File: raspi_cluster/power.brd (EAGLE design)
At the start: 28.9 x 34.3 mm, 5 parts

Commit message: made the printable pcb design
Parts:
- added 5V1, 5V2, 5V3, 5V4, 5V5: 22-23-2051, con-molex:22-23-2051
- added LED1, LED2, LED3, LED4, LED5: (no value), eagle-ltspice:LED_LD260
- added R1, R2, R3, R4, R5: (no value), resistor:0204/7
- added RASPI1, RASPI2, RASPI3, RASPI4, RASPI5: (no value), jumper:JP6Q
- added TYBG1, TYBG2, TYBG3, TYBG4, TYBG5: FUSEPICOFUSE, fuse:PICOFUSE
- moved TYBG 55.1 mm to (18.4, 11.1)
- moved 5V 55.1 mm to (8.26, 7.30)
- moved LED 55.1 mm to (4.45, 23.8)
- moved R 55.1 mm to (13.3, 23.8)
- moved RASPI 55.1 mm to (6.99, 14.9)
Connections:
- new net N$10: RASPI1.11, TYBG1.1
- new net N$11: 5V1.4, 5V1.5, RASPI1.7
- new net N$12: R1.2, RASPI1.12
- new net N$13: 5V2.1, 5V2.2, TYBG2.2
- new net N$14: LED2.A, R2.1
- new net N$15: LED2.K, RASPI2.8
- new net N$16: RASPI2.11, TYBG2.1
- new net N$17: 5V2.4, 5V2.5, RASPI2.7
- new net N$18: R2.2, RASPI2.12
- new net N$19: 5V3.1, 5V3.2, TYBG3.2
- new net N$20: LED3.A, R3.1
- new net N$21: LED3.K, RASPI3.8
- new net N$22: RASPI3.11, TYBG3.1
- new net N$23: 5V3.4, 5V3.5, RASPI3.7
- new net N$24: R3.2, RASPI3.12
- new net N$25: 5V4.1, 5V4.2, TYBG4.2
- new net N$26: LED4.A, R4.1
- new net N$27: LED4.K, RASPI4.8
- new net N$28: RASPI4.11, TYBG4.1
- new net N$29: 5V4.4, 5V4.5, RASPI4.7
- new net N$30: R4.2, RASPI4.12
- new net N$31: 5V5.1, 5V5.2, TYBG5.2
- new net N$32: LED5.A, R5.1
- new net N$33: LED5.K, RASPI5.8
- new net N$34: RASPI5.11, TYBG5.1
- new net N$35: 5V5.4, 5V5.5, RASPI5.7
- new net N$36: R5.2, RASPI5.12
- new net N$7: 5V1.1, 5V1.2, TYBG1.2
- new net N$8: LED1.A, R1.1
- new net N$9: LED1.K, RASPI1.8
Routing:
- net N$33: track 0.00 -> 11.7 mm, vias 0 -> 1
- net N$15: track 0.00 -> 11.7 mm, vias 0 -> 1
- net N$9: track 0.00 -> 11.7 mm, vias 0 -> 1
- net N$27: track 0.00 -> 11.7 mm, vias 0 -> 1
- net N$21: track 0.00 -> 11.7 mm, vias 0 -> 1
- net N$36: track 0.00 -> 9.94 mm
- net N$24: track 0.00 -> 9.94 mm
- net N$18: track 0.00 -> 9.94 mm
- net N$30: track 0.00 -> 9.94 mm
- net N$12: track 0.00 -> 9.94 mm
- net N$17: track 0.00 -> 9.36 mm
- net N$35: track 0.00 -> 9.36 mm
- net N$11: track 0.00 -> 9.36 mm
- net N$29: track 0.00 -> 9.36 mm
- net N$23: track 0.00 -> 9.36 mm
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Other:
- board size 28.9 x 34.3 mm -> 87.3 x 68.9 mm
- board text removed: "db tech"
- board text removed: "printed with love"

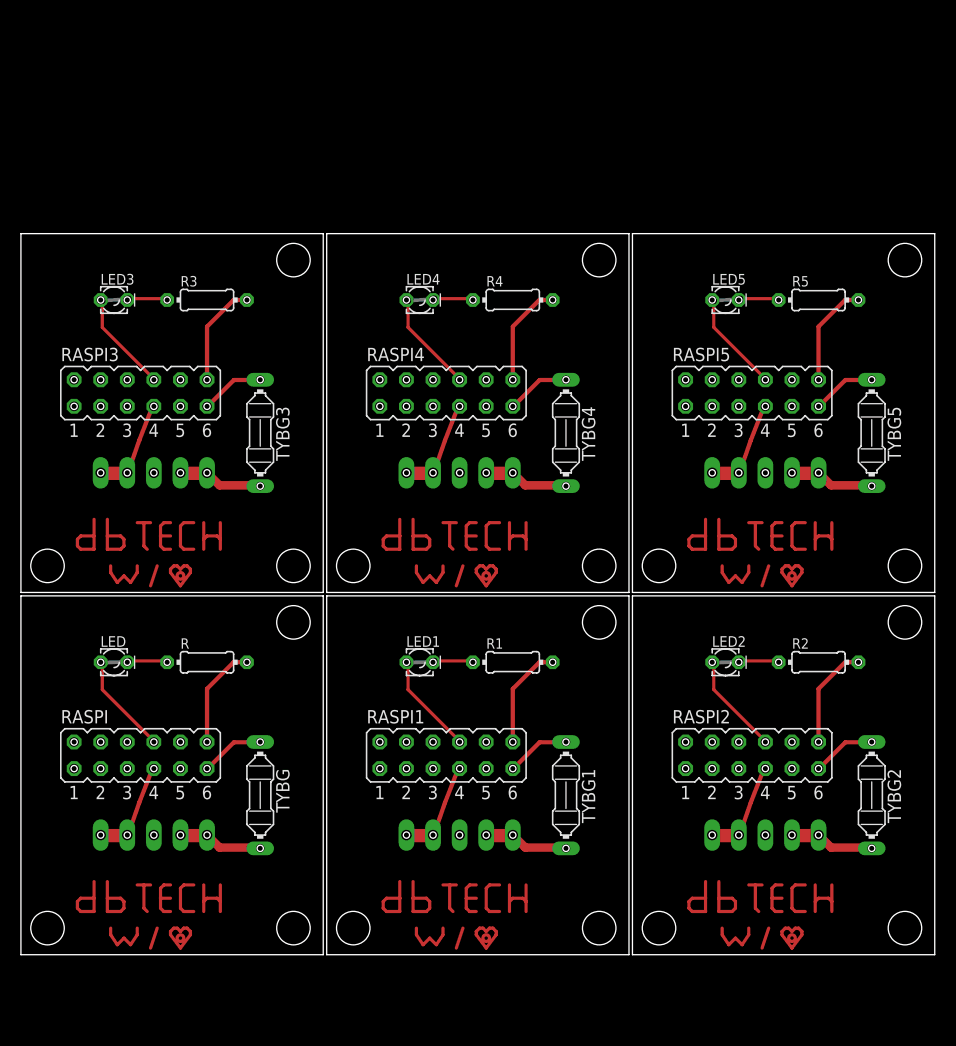
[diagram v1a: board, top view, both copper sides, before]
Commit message: updated power schematic for breakout board
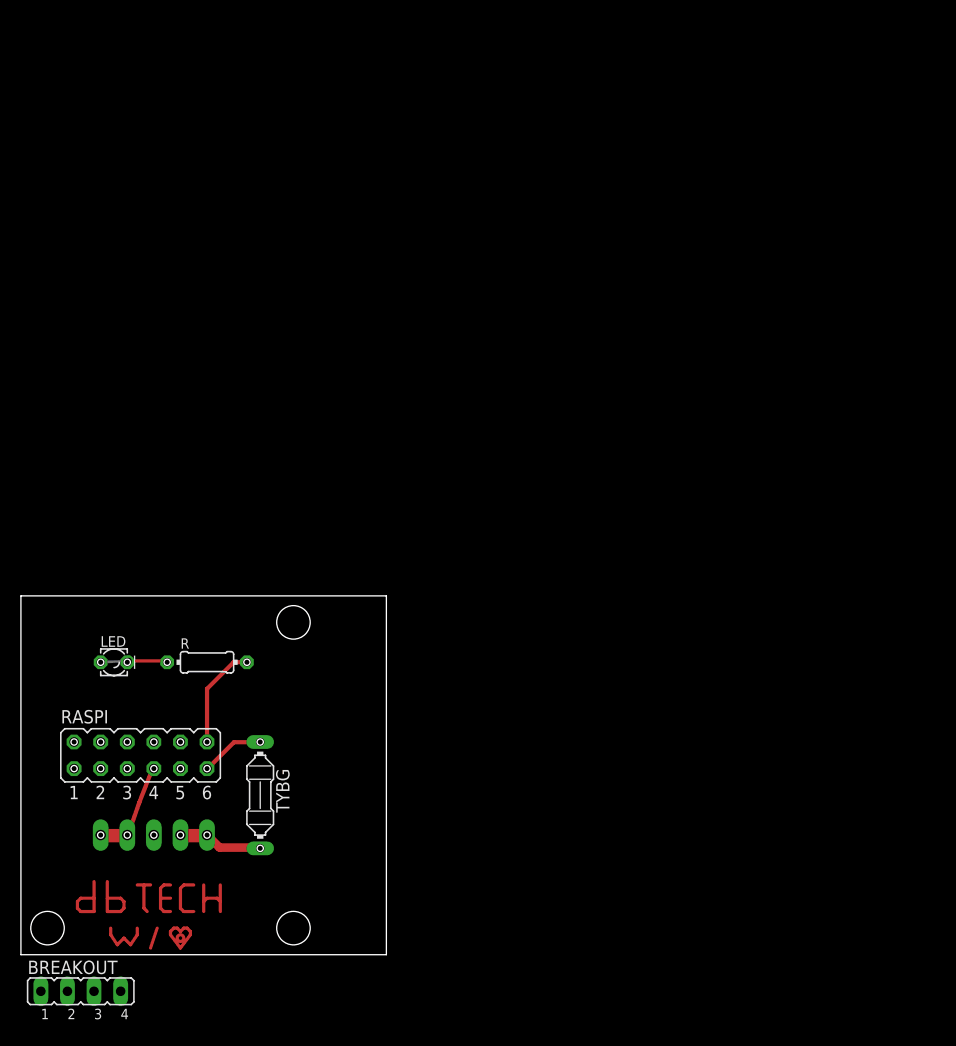
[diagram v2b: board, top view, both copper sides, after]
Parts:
- removed 5V1, 5V2, 5V3, 5V4, 5V5: 22-23-2051, con-molex:22-23-2051
- removed LED1, LED2, LED3, LED4, LED5: (no value), eagle-ltspice:LED_LD260
- removed R1, R2, R3, R4, R5: (no value), resistor:0204/7
- removed RASPI1, RASPI2, RASPI3, RASPI4, RASPI5: (no value), jumper:JP6Q
- removed TYBG1, TYBG2, TYBG3, TYBG4, TYBG5: FUSEPICOFUSE, fuse:PICOFUSE
- added BREAKOUT: (no value), jumper:JP4
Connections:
- removed net N$10: RASPI1.11, TYBG1.1
- removed net N$11: 5V1.4, 5V1.5, RASPI1.7
- removed net N$12: R1.2, RASPI1.12
- removed net N$13: 5V2.1, 5V2.2, TYBG2.2
- removed net N$14: LED2.A, R2.1
- removed net N$15: LED2.K, RASPI2.8
- removed net N$16: RASPI2.11, TYBG2.1
- removed net N$17: 5V2.4, 5V2.5, RASPI2.7
- removed net N$18: R2.2, RASPI2.12
- removed net N$19: 5V3.1, 5V3.2, TYBG3.2
- removed net N$20: LED3.A, R3.1
- removed net N$21: LED3.K, RASPI3.8
- removed net N$22: RASPI3.11, TYBG3.1
- removed net N$23: 5V3.4, 5V3.5, RASPI3.7
- removed net N$24: R3.2, RASPI3.12
- removed net N$25: 5V4.1, 5V4.2, TYBG4.2
- removed net N$26: LED4.A, R4.1
- removed net N$27: LED4.K, RASPI4.8
- removed net N$28: RASPI4.11, TYBG4.1
- removed net N$29: 5V4.4, 5V4.5, RASPI4.7
- removed net N$30: R4.2, RASPI4.12
- removed net N$31: 5V5.1, 5V5.2, TYBG5.2
- removed net N$32: LED5.A, R5.1
- removed net N$33: LED5.K, RASPI5.8
- removed net N$34: RASPI5.11, TYBG5.1
- removed net N$35: 5V5.4, 5V5.5, RASPI5.7
- removed net N$36: R5.2, RASPI5.12
- removed net N$8 (its old number): LED1.A, R1.1
- removed net N$9: LED1.K, RASPI1.8
- new net N$4: BREAKOUT.1
- net N$2: now also BREAKOUT.3
- net N$6: now also BREAKOUT.4
- net N$7: now also BREAKOUT.2; no longer 5V1.1, 5V1.2, TYBG1.2
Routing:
- net N$33: track 11.7 -> 0.00 mm, vias 1 -> 0
- net N$15: track 11.7 -> 0.00 mm, vias 1 -> 0
- net N$9: track 11.7 -> 0.00 mm, vias 1 -> 0
- net N$27: track 11.7 -> 0.00 mm, vias 1 -> 0
- net N$8: track 11.7 -> 0.00 mm, vias 1 -> 0
- net N$21: track 11.7 -> 0.00 mm, vias 1 -> 0
- net N$36: track 9.94 -> 0.00 mm
- net N$24: track 9.94 -> 0.00 mm
- net N$18: track 9.94 -> 0.00 mm
- net N$30: track 9.94 -> 0.00 mm
- net N$12: track 9.94 -> 0.00 mm
- net N$17: track 9.36 -> 0.00 mm
- net N$35: track 9.36 -> 0.00 mm
- net N$11: track 9.36 -> 0.00 mm
- net N$29: track 9.36 -> 0.00 mm
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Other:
- board size 87.3 x 68.9 mm -> 34.9 x 34.3 mm

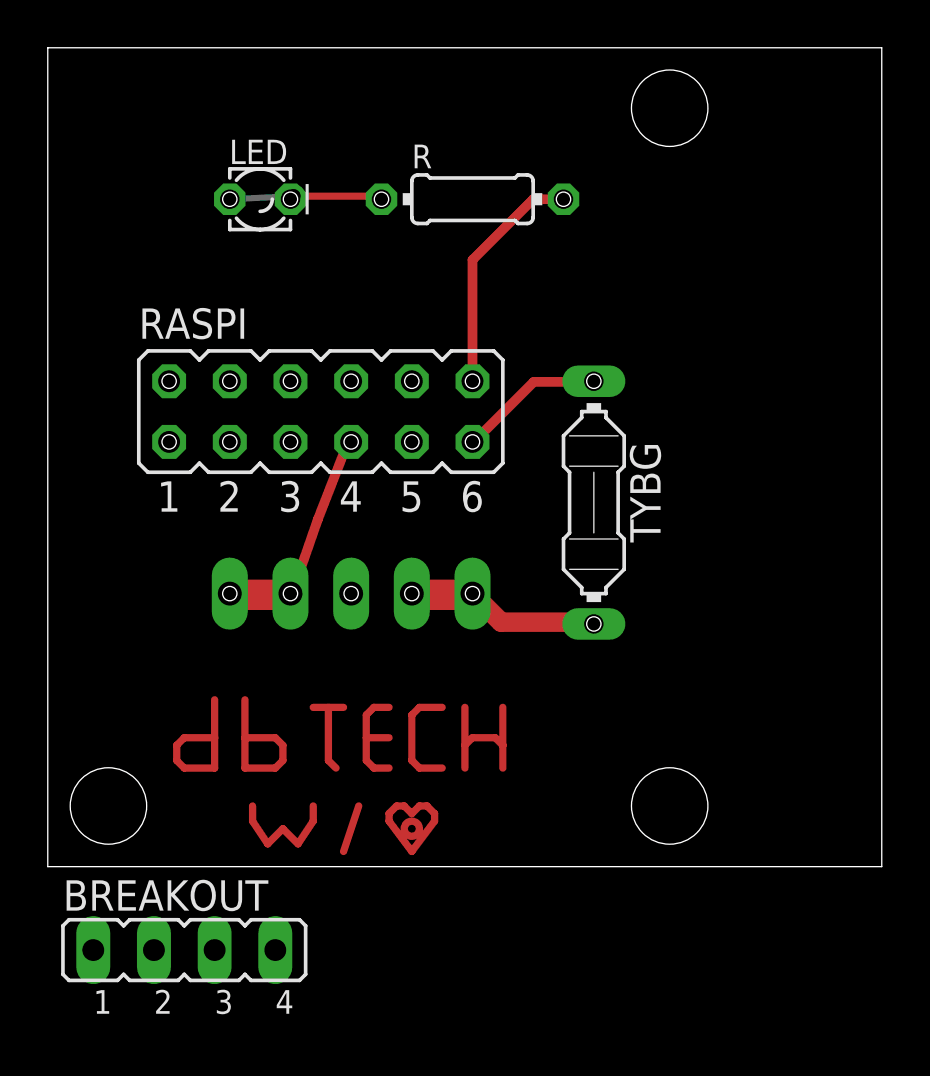
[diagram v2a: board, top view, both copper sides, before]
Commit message: New powerboard break out
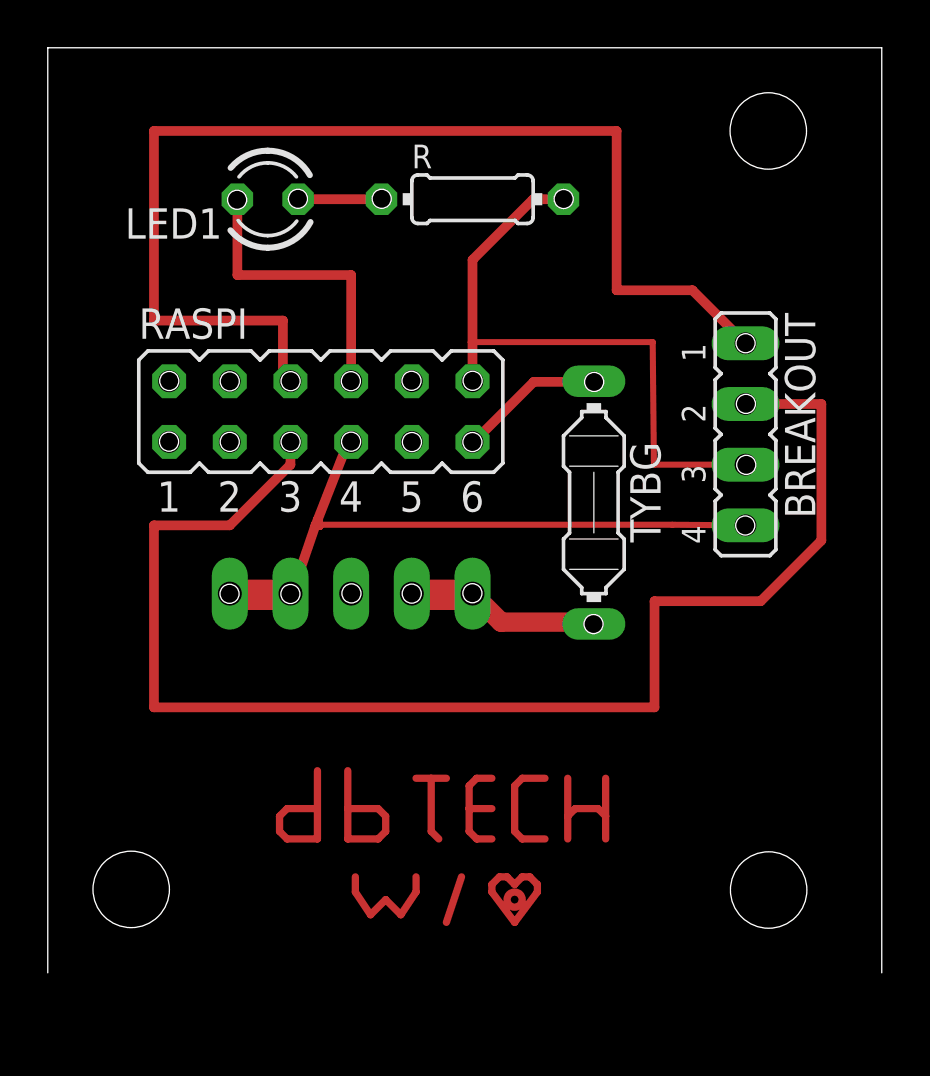
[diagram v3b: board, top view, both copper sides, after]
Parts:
- removed LED: (no value), eagle-ltspice:LED_LD260
- added LED1: TLLR4400, led:LED3MM
- moved BREAKOUT 31.9 mm to (24.8, 14.0), turned to 270 degrees
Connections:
- net N$3: now also LED1.A; no longer LED.A
- net N$4: now also RASPI.6
- net N$7: now also RASPI.5
- net N$8: now also LED1.K; no longer LED.K
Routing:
- net N$7: track 0.00 -> 57.7 mm
- net N$4: track 0.00 -> 48.5 mm
- net N$6: track 9.36 -> 28.0 mm
- net N$2: track 9.94 -> 26.5 mm
- net N$8: track 0.00 -> 12.4 mm
- net N$3: track 6.46 -> 3.49 mm, vias 1 -> 0
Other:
- board size 34.9 x 34.3 mm -> 34.9 x 38.7 mm
